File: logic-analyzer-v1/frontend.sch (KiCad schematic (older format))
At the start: 0 parts

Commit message: add comparator&sram
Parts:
- added U?: comp_LM239D, symbol New_Library:comp_LM239D
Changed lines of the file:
@@
 Wire Wire Line
 	1650 2350 2550 2350
+$Comp
+L New_Library:comp_LM239D U?
+U 1 1 6065525E
+P 6150 4450
+F 0 "U?" H 5475 5965 50  0000 C CNN
+F 1 "comp_LM239D" H 5475 5874 50  0000 C CNN
+F 2 "" H 6150 4450 50  0001 C CNN
+F 3 "" H 6150 4450 50  0001 C CNN
+	1    6150 4450
+	1    0    0    -1
+$EndComp
 $EndSCHEMATC

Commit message: MOD uart port direction, minor cosmetic changes
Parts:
- removed U?: comp_LM239D, symbol New_Library:comp_LM239D
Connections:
- net labels added: OUT[0..7]
- wire segments 8 -> 9
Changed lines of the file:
@@
 $Descr A4 11693 8268
 encoding utf-8
-Sheet 3 6
+Sheet 3 8
 Title ""
 Date ""
@@
 Wire Wire Line
 	1650 2350 2550 2350
-$Comp
-L New_Library:comp_LM239D U?
-U 1 1 6065525E
-P 6150 4450
-F 0 "U?" H 5475 5965 50  0000 C CNN
-F 1 "comp_LM239D" H 5475 5874 50  0000 C CNN
-F 2 "" H 6150 4450 50  0001 C CNN
-F 3 "" H 6150 4450 50  0001 C CNN
-	1    6150 4450
-	1    0    0    -1
-$EndComp
+Wire Wire Line
+	3800 2350 4600 2350
+Text HLabel 1900 4300 0    50   Output ~ 0
+OUT[0..7]
+$Sheet
+S 7300 1750 1250 950
+U 6085A2CD
+F0 "buffer_0" 50
+F1 "schmitt_trigger.sch" 50
+F2 "VREF_IN" I L 7300 1950 50
+F3 "VCC" U L 7300 1850 50
+F4 "GND" U L 7300 2600 50
+F5 "IN0" I R 8550 2100 50
+F6 "OUT0" O L 7300 2100 50
+F7 "OUT1" O L 7300 2200 50
+F8 "OUT2" O L 7300 2300 50
+F9 "OUT3" O L 7300 2400 50
+F10 "IN1" I R 8550 2200 50
+F11 "IN2" I R 8550 2300 50
+F12 "IN3" I R 8550 2400 50
+$EndSheet
+$Sheet
+S 7300 2950 1250 950
+U 6088C9AD
+F0 "buffer_1" 50
+F1 "schmitt_trigger.sch" 50
+F2 "VREF_IN" I L 7300 3150 50
+F3 "VCC" U L 7300 3050 50
+F4 "GND" U L 7300 3800 50
+F5 "IN0" I R 8550 3300 50
+F6 "OUT0" O L 7300 3300 50
+F7 "OUT1" O L 7300 3400 50
+F8 "OUT2" O L 7300 3500 50
+F9 "OUT3" O L 7300 3600 50
+F10 "IN1" I R 8550 3400 50
+F11 "IN2" I R 8550 3500 50
+F12 "IN3" I R 8550 3600 50
+$EndSheet
 $EndSCHEMATC

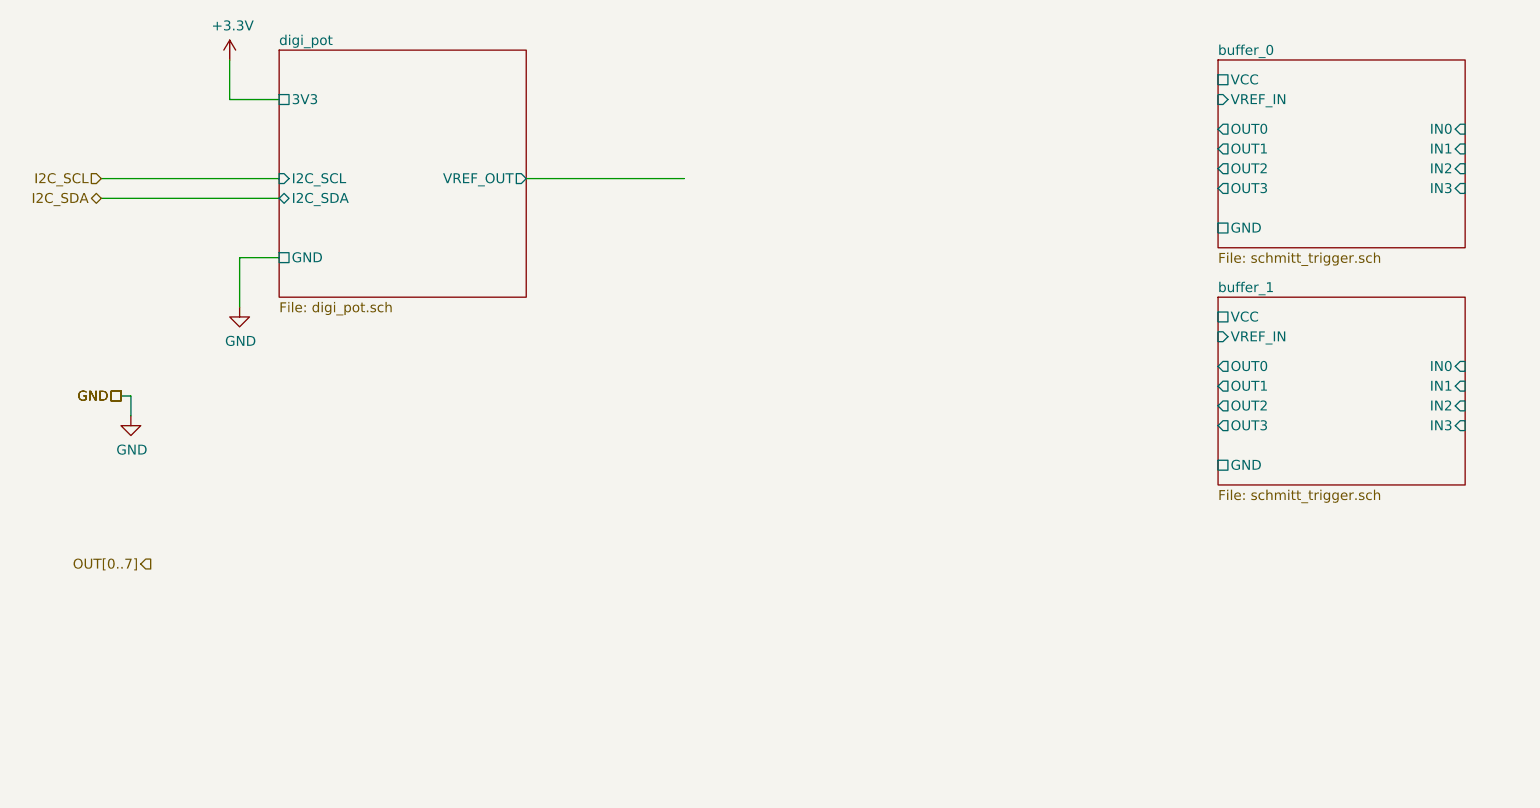
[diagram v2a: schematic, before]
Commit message: changing sram blocks from new library
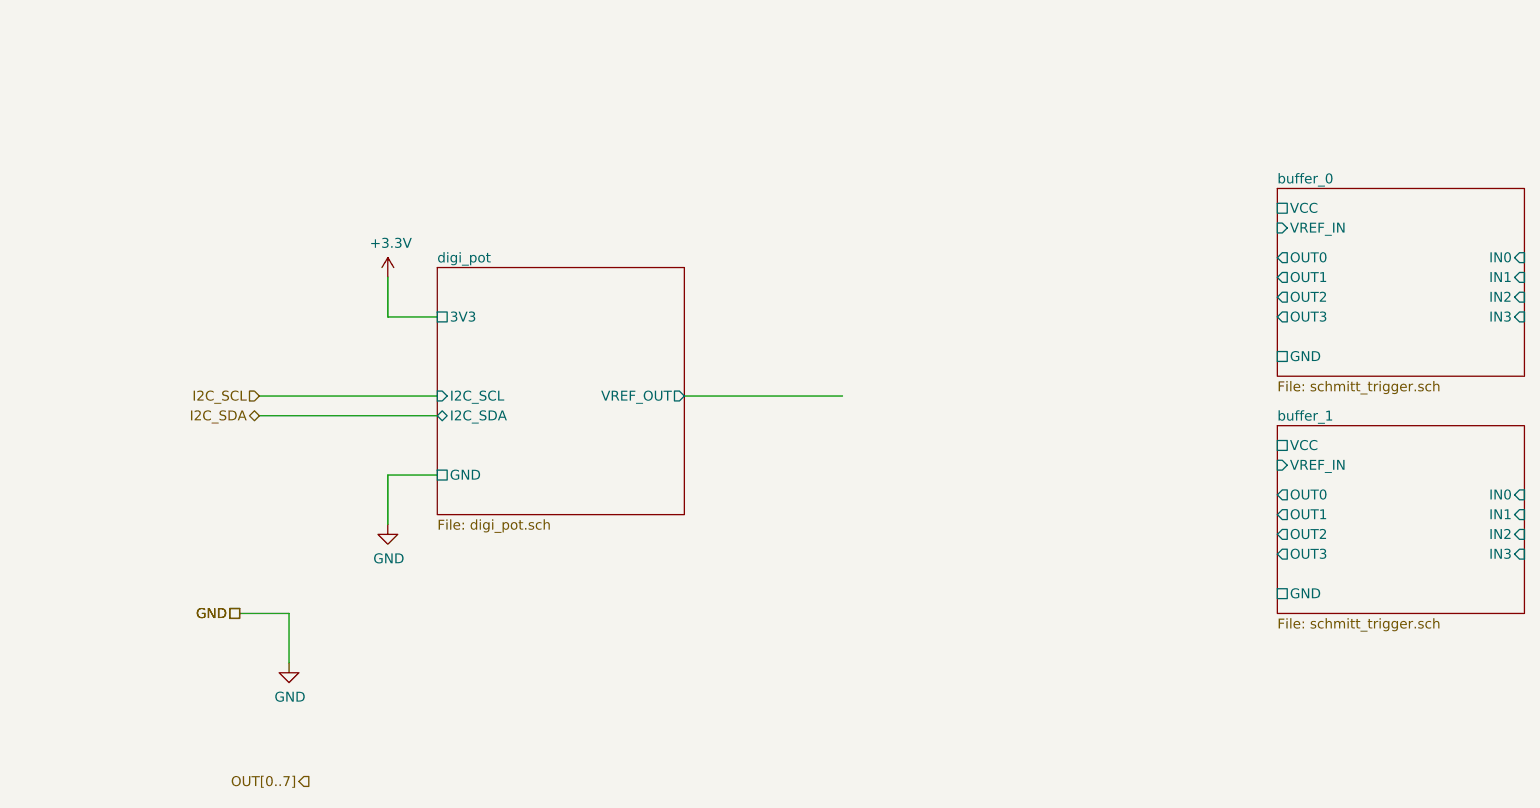
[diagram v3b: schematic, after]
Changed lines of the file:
@@
 Comment4 ""
 $EndDescr
-Text HLabel 1750 3450 0    50   UnSpc ~ 0
+Text HLabel 2350 4550 0    50   UnSpc ~ 0
 GND
-Text HLabel 1750 3450 0    50   UnSpc ~ 0
+Text HLabel 2350 4550 0    50   UnSpc ~ 0
 GND
 $Sheet
-S 2550 1700 1250 1250
+S 3350 2800 1250 1250
 U 5FDA8D6E
 F0 "digi_pot" 50
 F1 "digi_pot.sch" 50
-F2 "VREF_OUT" O R 3800 2350 50
-F3 "3V3" U L 2550 1950 50
-F4 "GND" U L 2550 2750 50
-F5 "I2C_SCL" I L 2550 2350 50
-F6 "I2C_SDA" B L 2550 2450 50
+F2 "VREF_OUT" O R 4600 3450 50
+F3 "3V3" U L 3350 3050 50
+F4 "GND" U L 3350 3850 50
+F5 "I2C_SCL" I L 3350 3450 50
+F6 "I2C_SDA" B L 3350 3550 50
 $EndSheet
 $Comp
 L power:GND #PWR?
 U 1 1 5FDA9780
-P 2350 3000
-F 0 "#PWR?" H 2350 2750 50  0001 C CNN
-F 1 "GND" H 2355 2827 50  0000 C CNN
-F 2 "" H 2350 3000 50  0001 C CNN
-F 3 "" H 2350 3000 50  0001 C CNN
-	1    2350 3000
+P 3100 4100
+F 0 "#PWR?" H 3100 3850 50  0001 C CNN
+F 1 "GND" H 3105 3927 50  0000 C CNN
+F 2 "" H 3100 4100 50  0001 C CNN
+F 3 "" H 3100 4100 50  0001 C CNN
+	1    3100 4100
 	1    0    0    -1
 $EndComp
 Wire Wire Line
-	2550 2750 2350 2750
-Wire Wire Line
-	2350 2750 2350 3000
+	3100 3850 3100 4100
 $Comp
 L power:GND #PWR?
 U 1 1 5FDAB2A6
-P 1800 3550
-F 0 "#PWR?" H 1800 3300 50  0001 C CNN
-F 1 "GND" H 1805 3377 50  0000 C CNN
-F 2 "" H 1800 3550 50  0001 C CNN
-F 3 "" H 1800 3550 50  0001 C CNN
-	1    1800 3550
+P 2600 4800
+F 0 "#PWR?" H 2600 4550 50  0001 C CNN
+F 1 "GND" H 2605 4627 50  0000 C CNN
+F 2 "" H 2600 4800 50  0001 C CNN
+F 3 "" H 2600 4800 50  0001 C CNN
+	1    2600 4800
 	1    0    0    -1
 $EndComp
 Wire Wire Line
-	1750 3450 1800 3450
-Wire Wire Line
-	1800 3450 1800 3550
+	2600 4550 2600 4800
 $Comp
 L power:+3.3V #PWR?
 U 1 1 5FDABC64
-P 2300 1750
-F 0 "#PWR?" H 2300 1600 50  0001 C CNN
-F 1 "+3.3V" H 2315 1923 50  0000 C CNN
-F 2 "" H 2300 1750 50  0001 C CNN
-F 3 "" H 2300 1750 50  0001 C CNN
-	1    2300 1750
+P 3100 2850
+F 0 "#PWR?" H 3100 2700 50  0001 C CNN
+F 1 "+3.3V" H 3115 3023 50  0000 C CNN
+F 2 "" H 3100 2850 50  0001 C CNN
+F 3 "" H 3100 2850 50  0001 C CNN
+	1    3100 2850
 	1    0    0    -1
 $EndComp
 Wire Wire Line
-	2550 1950 2300 1950
+	3350 3050 3100 3050
 Wire Wire Line
-	2300 1950 2300 1750
-Text HLabel 1650 2350 0    50   Input ~ 0
+	3100 3050 3100 2850
+Text HLabel 2450 3450 0    50   Input ~ 0
 I2C_SCL
-Text HLabel 1650 2450 0    50   BiDi ~ 0
+Text HLabel 2450 3550 0    50   BiDi ~ 0
 I2C_SDA
 Wire Wire Line
-	1650 2450 2550 2450
+	2450 3550 3350 3550
 Wire Wire Line
-	1650 2350 2550 2350
+	2450 3450 3350 3450
 Wire Wire Line
-	3800 2350 4600 2350
-Text HLabel 1900 4300 0    50   Output ~ 0
+	4600 3450 5400 3450
+Text HLabel 2700 5400 0    50   Output ~ 0
 OUT[0..7]
 $Sheet
-S 7300 1750 1250 950
+S 7600 2400 1250 950
 U 6085A2CD
 F0 "buffer_0" 50
 F1 "schmitt_trigger.sch" 50
-F2 "VREF_IN" I L 7300 1950 50
-F3 "VCC" U L 7300 1850 50
-F4 "GND" U L 7300 2600 50
-F5 "IN0" I R 8550 2100 50
-F6 "OUT0" O L 7300 2100 50
-F7 "OUT1" O L 7300 2200 50
-F8 "OUT2" O L 7300 2300 50
-F9 "OUT3" O L 7300 2400 50
-F10 "IN1" I R 8550 2200 50
-F11 "IN2" I R 8550 2300 50
-F12 "IN3" I R 8550 2400 50
+F2 "VREF_IN" I L 7600 2600 50
+F3 "VCC" U L 7600 2500 50
+F4 "GND" U L 7600 3250 50
+F5 "IN0" I R 8850 2750 50
+F6 "OUT0" O L 7600 2750 50
+F7 "OUT1" O L 7600 2850 50
+F8 "OUT2" O L 7600 2950 50
+F9 "OUT3" O L 7600 3050 50
+F10 "IN1" I R 8850 2850 50
+F11 "IN2" I R 8850 2950 50
+F12 "IN3" I R 8850 3050 50
 $EndSheet
 $Sheet
-S 7300 2950 1250 950
+S 7600 3600 1250 950
 U 6088C9AD
 F0 "buffer_1" 50
 F1 "schmitt_trigger.sch" 50
-F2 "VREF_IN" I L 7300 3150 50
-F3 "VCC" U L 7300 3050 50
-F4 "GND" U L 7300 3800 50
-F5 "IN0" I R 8550 3300 50
-F6 "OUT0" O L 7300 3300 50
-F7 "OUT1" O L 7300 3400 50
-F8 "OUT2" O L 7300 3500 50
-F9 "OUT3" O L 7300 3600 50
-F10 "IN1" I R 8550 3400 50
-F11 "IN2" I R 8550 3500 50
-F12 "IN3" I R 8550 3600 50
+F2 "VREF_IN" I L 7600 3800 50
+F3 "VCC" U L 7600 3700 50
+F4 "GND" U L 7600 4450 50
+F5 "IN0" I R 8850 3950 50
+F6 "OUT0" O L 7600 3950 50
+F7 "OUT1" O L 7600 4050 50
+F8 "OUT2" O L 7600 4150 50
+F9 "OUT3" O L 7600 4250 50
+F10 "IN1" I R 8850 4050 50
+F11 "IN2" I R 8850 4150 50
+F12 "IN3" I R 8850 4250 50
 $EndSheet
+Wire Wire Line
+	2350 4550 2600 4550
+Wire Wire Line
+	3100 3850 3350 3850
 $EndSCHEMATC

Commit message: delete old sram
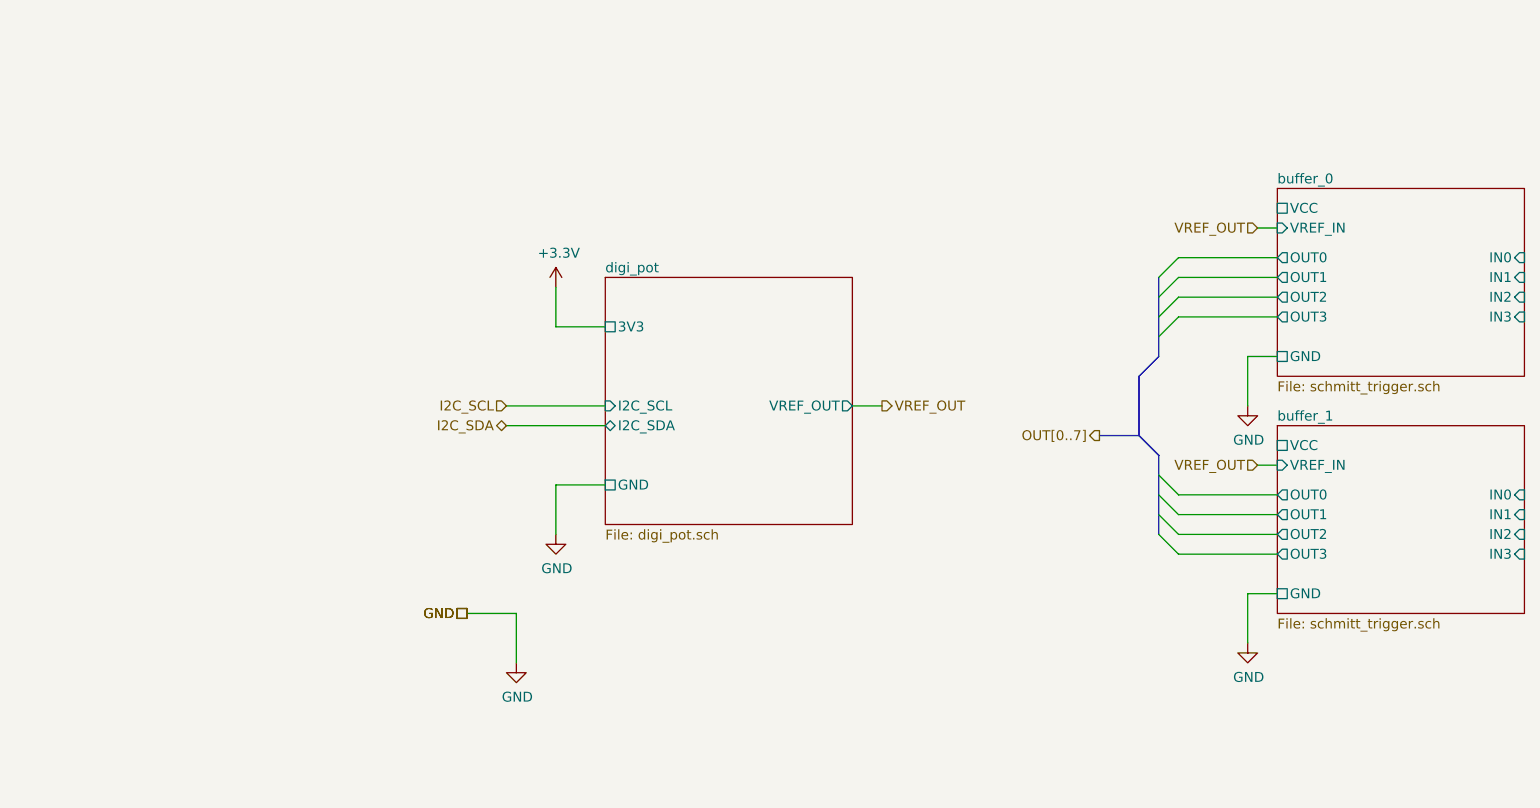
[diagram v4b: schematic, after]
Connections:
- net labels added: VREF_OUT
- wire segments 9 -> 23
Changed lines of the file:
@@
 Comment4 ""
 $EndDescr
-Text HLabel 2350 4550 0    50   UnSpc ~ 0
-GND
-Text HLabel 2350 4550 0    50   UnSpc ~ 0
-GND
-$Sheet
-S 3350 2800 1250 1250
-U 5FDA8D6E
-F0 "digi_pot" 50
-F1 "digi_pot.sch" 50
-F2 "VREF_OUT" O R 4600 3450 50
-F3 "3V3" U L 3350 3050 50
-F4 "GND" U L 3350 3850 50
-F5 "I2C_SCL" I L 3350 3450 50
-F6 "I2C_SDA" B L 3350 3550 50
-$EndSheet
-$Comp
-L power:GND #PWR?
-U 1 1 5FDA9780
-P 3100 4100
-F 0 "#PWR?" H 3100 3850 50  0001 C CNN
-F 1 "GND" H 3105 3927 50  0000 C CNN
-F 2 "" H 3100 4100 50  0001 C CNN
-F 3 "" H 3100 4100 50  0001 C CNN
-	1    3100 4100
-	1    0    0    -1
-$EndComp
-Wire Wire Line
-	3100 3850 3100 4100
-$Comp
-L power:GND #PWR?
-U 1 1 5FDAB2A6
-P 2600 4800
-F 0 "#PWR?" H 2600 4550 50  0001 C CNN
-F 1 "GND" H 2605 4627 50  0000 C CNN
-F 2 "" H 2600 4800 50  0001 C CNN
-F 3 "" H 2600 4800 50  0001 C CNN
-	1    2600 4800
-	1    0    0    -1
-$EndComp
-Wire Wire Line
-	2600 4550 2600 4800
-$Comp
-L power:+3.3V #PWR?
-U 1 1 5FDABC64
-P 3100 2850
-F 0 "#PWR?" H 3100 2700 50  0001 C CNN
-F 1 "+3.3V" H 3115 3023 50  0000 C CNN
-F 2 "" H 3100 2850 50  0001 C CNN
-F 3 "" H 3100 2850 50  0001 C CNN
-	1    3100 2850
-	1    0    0    -1
-$EndComp
-Wire Wire Line
-	3350 3050 3100 3050
-Wire Wire Line
-	3100 3050 3100 2850
-Text HLabel 2450 3450 0    50   Input ~ 0
-I2C_SCL
-Text HLabel 2450 3550 0    50   BiDi ~ 0
-I2C_SDA
-Wire Wire Line
-	2450 3550 3350 3550
-Wire Wire Line
-	2450 3450 3350 3450
-Wire Wire Line
-	4600 3450 5400 3450
-Text HLabel 2700 5400 0    50   Output ~ 0
-OUT[0..7]
 $Sheet
 S 7600 2400 1250 950
@@
 F12 "IN3" I R 8850 4250 50
 $EndSheet
+Text HLabel 7500 2600 0    50   Input ~ 0
+VREF_OUT
+Text HLabel 7500 3800 0    50   Input ~ 0
+VREF_OUT
 Wire Wire Line
-	2350 4550 2600 4550
+	7600 2600 7500 2600
 Wire Wire Line
-	3100 3850 3350 3850
+	7600 3800 7500 3800
+$Comp
+L power:GND #PWR?
+U 1 1 6095AB44
+P 7450 4700
+F 0 "#PWR?" H 7450 4450 50  0001 C CNN
+F 1 "GND" H 7455 4527 50  0000 C CNN
+F 2 "" H 7450 4700 50  0001 C CNN
+F 3 "" H 7450 4700 50  0001 C CNN
+	1    7450 4700
+	1    0    0    -1
+$EndComp
+Wire Wire Line
+	7450 4450 7450 4700
+$Comp
+L power:GND #PWR?
+U 1 1 6095B05A
+P 7450 3500
+F 0 "#PWR?" H 7450 3250 50  0001 C CNN
+F 1 "GND" H 7455 3327 50  0000 C CNN
+F 2 "" H 7450 3500 50  0001 C CNN
+F 3 "" H 7450 3500 50  0001 C CNN
+	1    7450 3500
+	1    0    0    -1
+$EndComp
+Wire Wire Line
+	7450 3250 7450 3500
+Wire Wire Line
+	7450 3250 7600 3250
+Wire Wire Line
+	7450 4450 7600 4450
+Wire Wire Line
+	7100 2850 7600 2850
+Wire Wire Line
+	7100 2950 7600 2950
+Wire Wire Line
+	7100 3050 7600 3050
+Wire Wire Line
+	7100 3950 7600 3950
+Wire Wire Line
+	7100 4050 7600 4050
+Wire Wire Line
+	7100 4150 7600 4150
+Wire Wire Line
+	7100 4250 7600 4250
+Entry Wire Line
+	7000 3150 7100 3050
+Entry Wire Line
+	7000 3050 7100 2950
+Entry Wire Line
+	7000 2950 7100 2850
+Entry Wire Line
+	7000 2850 7100 2750
+Entry Wire Line
+	7000 3850 7100 3950
+Entry Wire Line
+	7000 3950 7100 4050
+Entry Wire Line
+	7000 4050 7100 4150
+Entry Wire Line
+	7000 4150 7100 4250
+Entry Bus Bus
+	7000 3250 6900 3350
+Entry Bus Bus
+	7000 3750 6900 3650
+Entry Bus Bus
+	6900 3650 7000 3750
+Wire Bus Line
+	6900 3350 6900 3650
+Wire Bus Line
+	6900 3650 6700 3650
+Text HLabel 6700 3650 0    50   Output ~ 0
+OUT[0..7]
+Text HLabel 3500 4550 0    50   UnSpc ~ 0
+GND
+Text HLabel 3500 4550 0    50   UnSpc ~ 0
+GND
+$Sheet
+S 4200 2850 1250 1250
+U 5FDA8D6E
+F0 "digi_pot" 50
+F1 "digi_pot.sch" 50
+F2 "VREF_OUT" O R 5450 3500 50
+F3 "3V3" U L 4200 3100 50
+F4 "GND" U L 4200 3900 50
+F5 "I2C_SCL" I L 4200 3500 50
+F6 "I2C_SDA" B L 4200 3600 50
+$EndSheet
+$Comp
+L power:GND #PWR?
+U 1 1 5FDA9780
+P 3950 4150
+F 0 "#PWR?" H 3950 3900 50  0001 C CNN
+F 1 "GND" H 3955 3977 50  0000 C CNN
+F 2 "" H 3950 4150 50  0001 C CNN
+F 3 "" H 3950 4150 50  0001 C CNN
+	1    3950 4150
+	1    0    0    -1
+$EndComp
+Wire Wire Line
+	3950 3900 3950 4150
+$Comp
+L power:GND #PWR?
+U 1 1 5FDAB2A6
+P 3750 4800
+F 0 "#PWR?" H 3750 4550 50  0001 C CNN
+F 1 "GND" H 3755 4627 50  0000 C CNN
+F 2 "" H 3750 4800 50  0001 C CNN
+F 3 "" H 3750 4800 50  0001 C CNN
+	1    3750 4800
+	1    0    0    -1
+$EndComp
+Wire Wire Line
+	3750 4550 3750 4800
+$Comp
+L power:+3.3V #PWR?
+U 1 1 5FDABC64
+P 3950 2900
+F 0 "#PWR?" H 3950 2750 50  0001 C CNN
+F 1 "+3.3V" H 3965 3073 50  0000 C CNN
+F 2 "" H 3950 2900 50  0001 C CNN
+F 3 "" H 3950 2900 50  0001 C CNN
+	1    3950 2900
+	1    0    0    -1
+$EndComp
+Wire Wire Line
+	4200 3100 3950 3100
+Wire Wire Line
+	3950 3100 3950 2900
+Text HLabel 3700 3500 0    50   Input ~ 0
+I2C_SCL
+Text HLabel 3700 3600 0    50   BiDi ~ 0
+I2C_SDA
+Wire Wire Line
+	3700 3600 4200 3600
+Wire Wire Line
+	3700 3500 4200 3500
+Wire Wire Line
+	5450 3500 5600 3500
+Wire Wire Line
+	3500 4550 3750 4550
+Wire Wire Line
+	3950 3900 4200 3900
+Text HLabel 5600 3500 2    50   Output ~ 0
+VREF_OUT
+Wire Bus Line
+	7000 3750 7000 4150
+Wire Bus Line
+	7000 2850 7000 3250
+Wire Wire Line
+	7100 2750 7600 2750
 $EndSCHEMATC
